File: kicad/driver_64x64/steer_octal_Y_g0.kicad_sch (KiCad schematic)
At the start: 66 parts

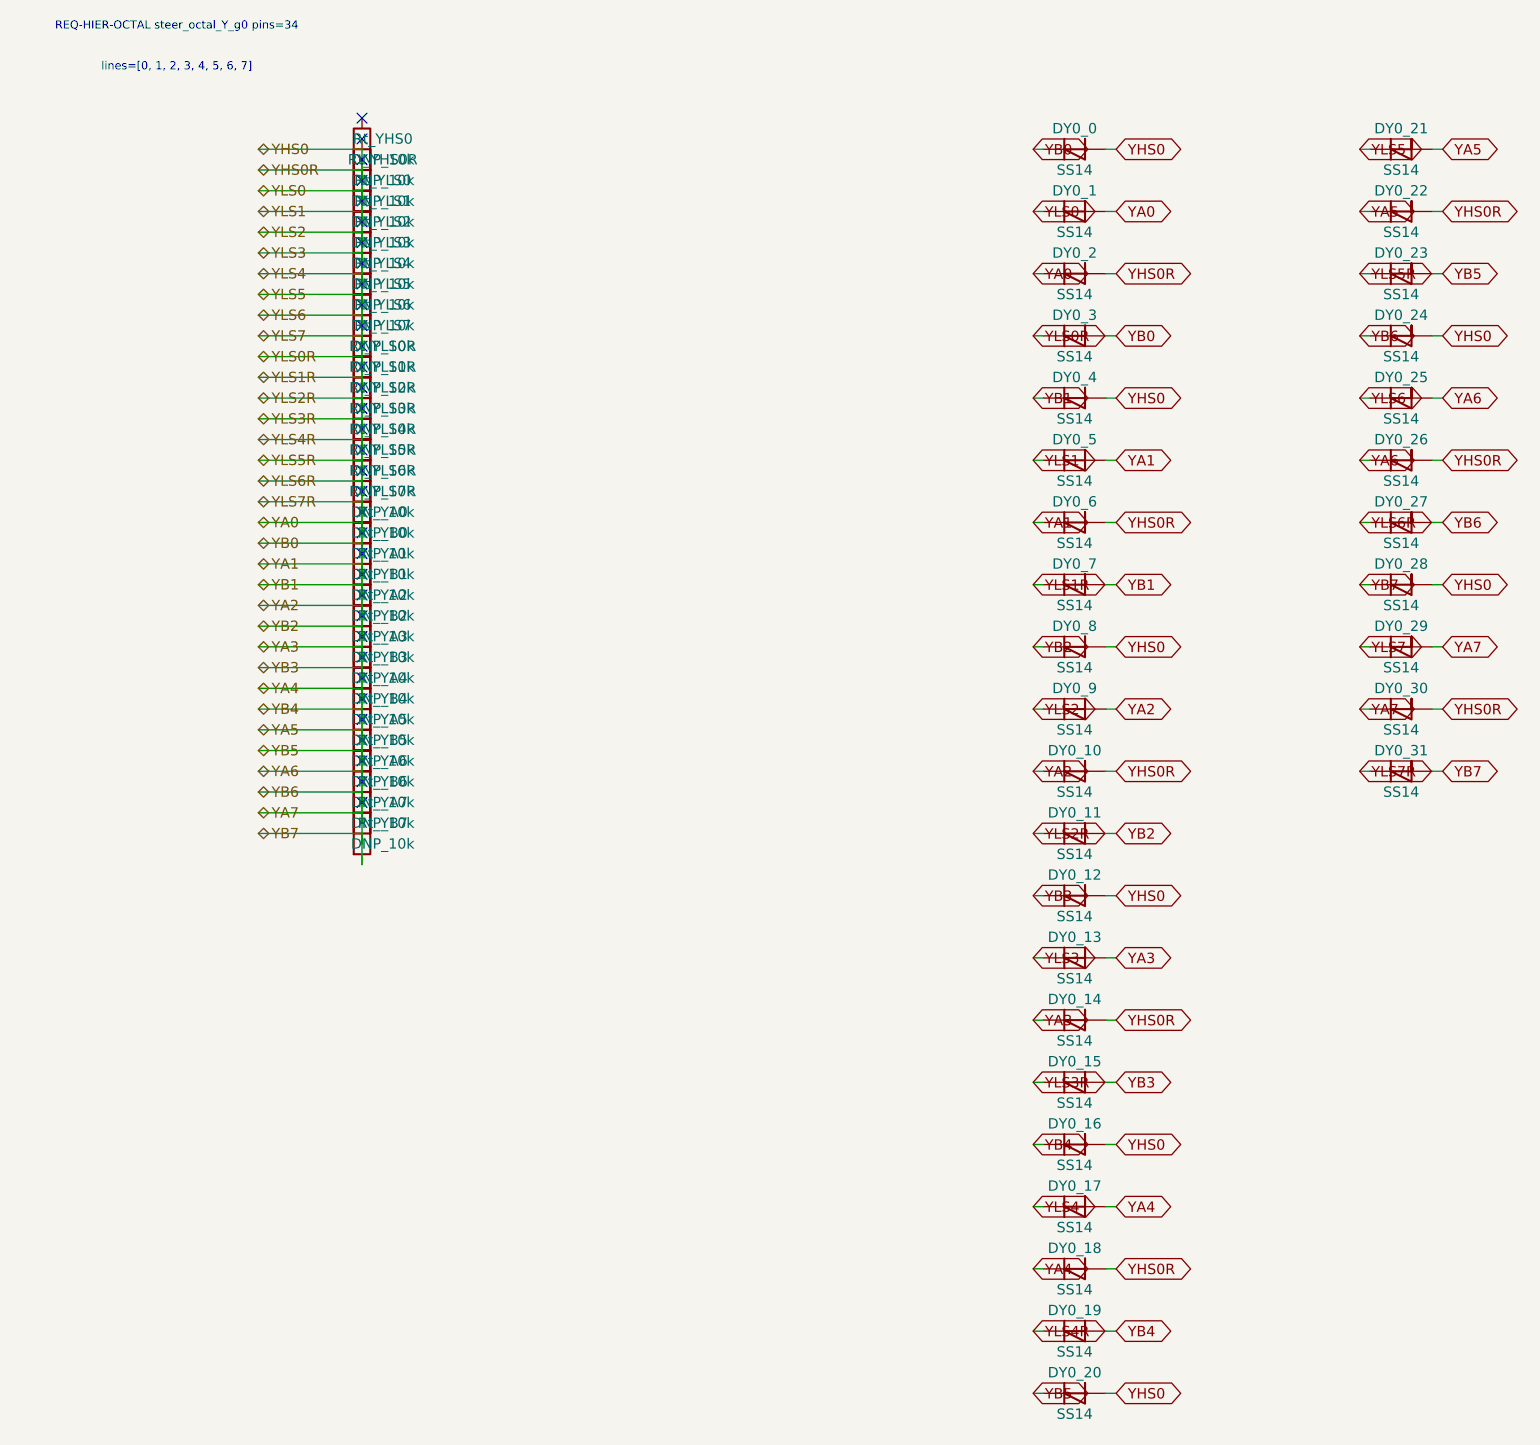
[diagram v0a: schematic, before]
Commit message: logical seperation into host and multiple decode/drive/steering boards
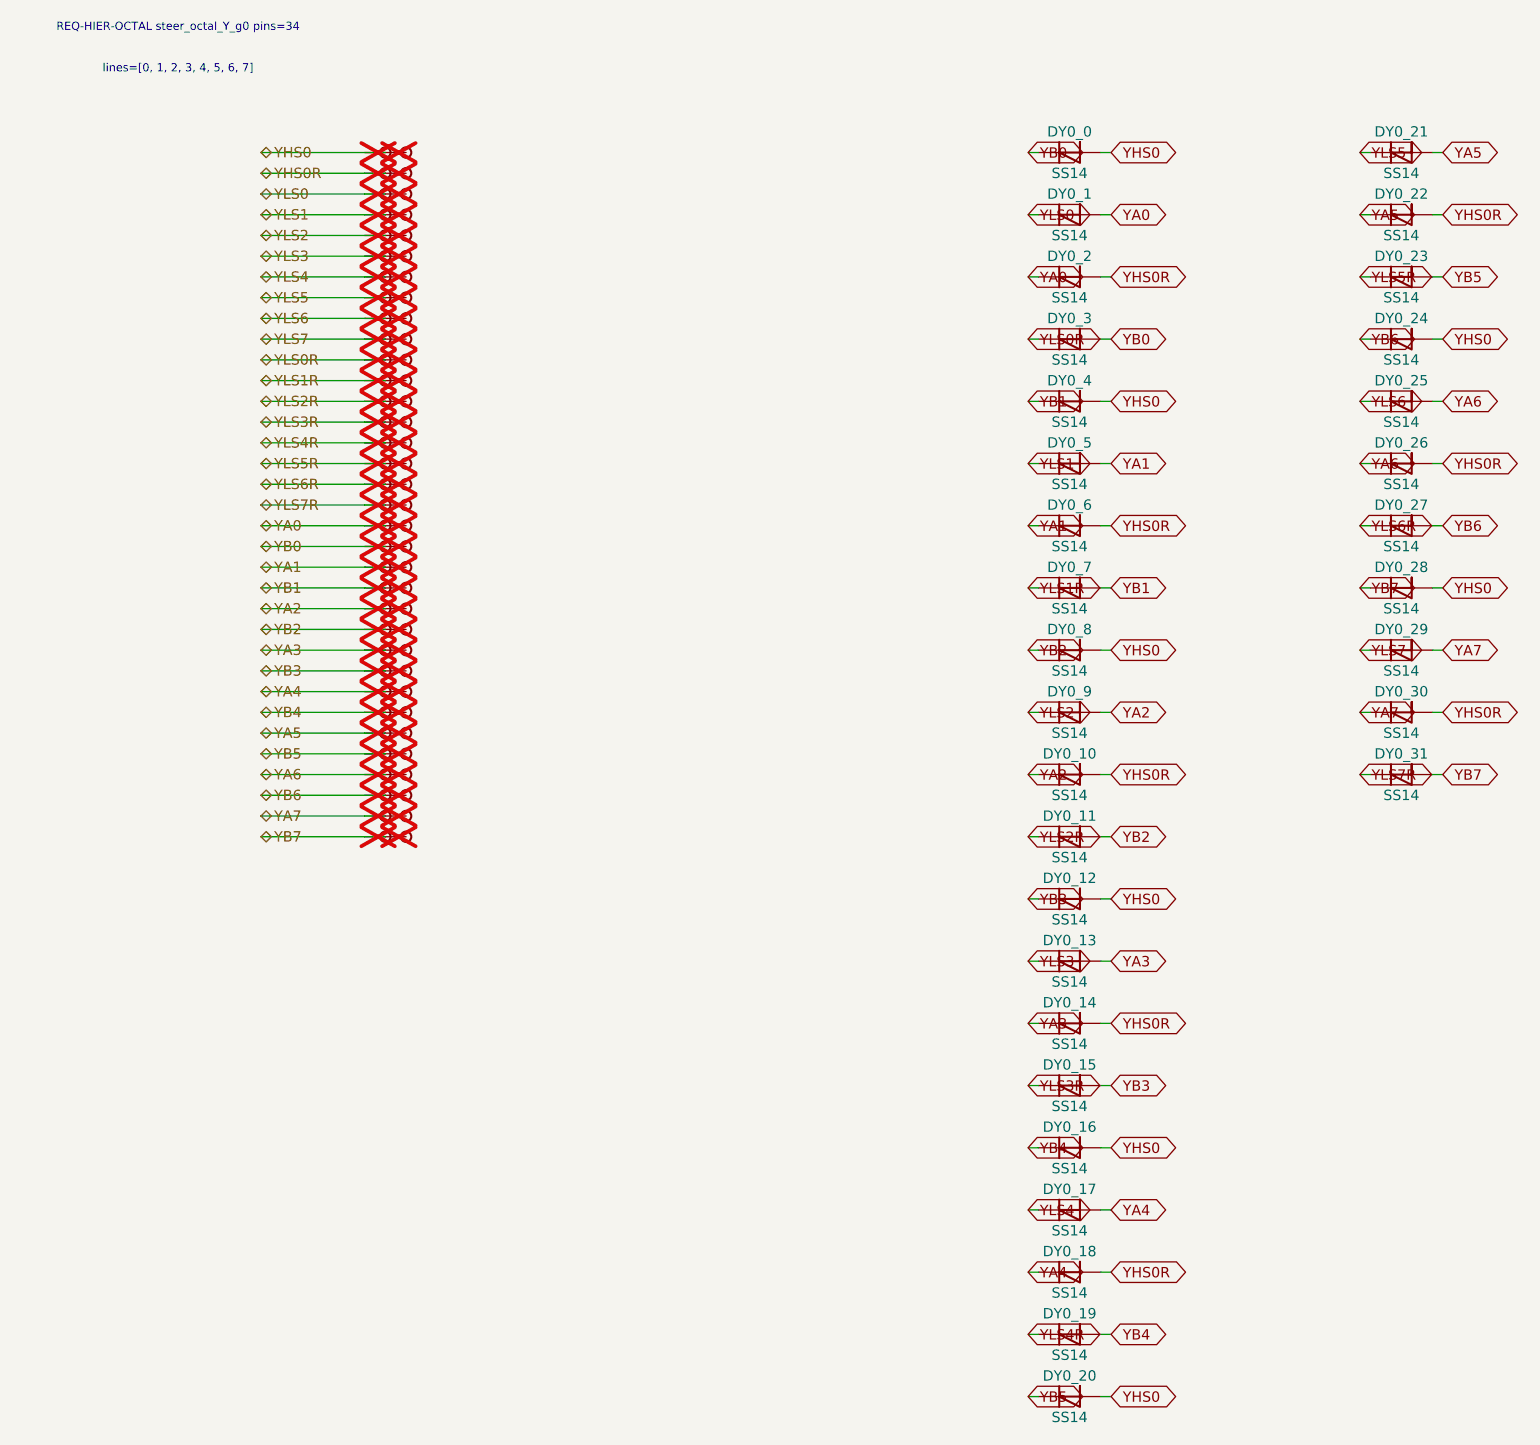
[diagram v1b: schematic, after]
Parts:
- removed Rt_YA0, Rt_YA1, Rt_YA2, Rt_YA3, Rt_YA4, Rt_YA5, Rt_YA6, Rt_YA7, Rt_YB0, Rt_YB1, Rt_YB2, Rt_YB3, Rt_YB4, Rt_YB5, Rt_YB6, Rt_YB7, Rt_YHS0, Rt_YHS0R, Rt_YLS0, Rt_YLS0R, Rt_YLS1, Rt_YLS1R, Rt_YLS2, Rt_YLS2R, Rt_YLS3, Rt_YLS3R, Rt_YLS4, Rt_YLS4R, Rt_YLS5, Rt_YLS5R, Rt_YLS6, Rt_YLS6R, Rt_YLS7, Rt_YLS7R: DNP_10k, symbol Device:R
- added TP_YA0, TP_YA0b, TP_YA1, TP_YA1b, TP_YA2, TP_YA2b, TP_YA3, TP_YA3b, TP_YA4, TP_YA4b, TP_YA5, TP_YA5b, TP_YA6, TP_YA6b, TP_YA7, TP_YA7b, TP_YB0, TP_YB0b, TP_YB1, TP_YB1b, TP_YB2, TP_YB2b, TP_YB3, TP_YB3b, TP_YB4, TP_YB4b, TP_YB5, TP_YB5b, TP_YB6, TP_YB6b, TP_YB7, TP_YB7b, TP_YHS0, TP_YHS0R, TP_YHS0Rb, TP_YHS0b, TP_YLS0, TP_YLS0R, TP_YLS0Rb, TP_YLS0b, TP_YLS1, TP_YLS1R, TP_YLS1Rb, TP_YLS1b, TP_YLS2, TP_YLS2R, TP_YLS2Rb, TP_YLS2b, TP_YLS3, TP_YLS3R, TP_YLS3Rb, TP_YLS3b, TP_YLS4, TP_YLS4R, TP_YLS4Rb, TP_YLS4b, TP_YLS5, TP_YLS5R, TP_YLS5Rb, TP_YLS5b, TP_YLS6, TP_YLS6R, TP_YLS6Rb, TP_YLS6b, TP_YLS7, TP_YLS7R, TP_YLS7Rb, TP_YLS7b: Stub, symbol CMR:Stub
- DY0_0, DY0_1, DY0_10, DY0_11, DY0_12, DY0_13, DY0_14, DY0_15, DY0_16, DY0_17, DY0_18, DY0_19, DY0_2, DY0_20, DY0_21, DY0_22, DY0_23, DY0_24, DY0_25, DY0_26, DY0_27, DY0_28, DY0_29, DY0_3, DY0_30, DY0_31, DY0_4, DY0_5, DY0_6, DY0_7, DY0_8, DY0_9: symbol Device:D_Schottky -> CMR:D_Schottky
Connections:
- net YA0: now also TP_YA0.1, TP_YA0b.1; no longer DY0_0.1 (K), DY0_0.2 (A), DY0_1.1 (K), DY0_10.1 (K), DY0_10.2 (A), DY0_11.1 (K), DY0_11.2 (A), DY0_12.1 (K), DY0_12.2 (A), DY0_13.1 (K), DY0_13.2 (A), DY0_14.1 (K), DY0_14.2 (A), DY0_15.1 (K), DY0_15.2 (A), DY0_16.1 (K), DY0_16.2 (A), DY0_17.1 (K), DY0_17.2 (A), DY0_18.1 (K), DY0_18.2 (A), DY0_19.1 (K), DY0_19.2 (A), DY0_2.2 (A), DY0_20.1 (K), DY0_20.2 (A), DY0_21.1 (K), DY0_21.2 (A), DY0_22.1 (K), DY0_22.2 (A), DY0_23.1 (K), DY0_23.2 (A), DY0_24.1 (K), DY0_24.2 (A), DY0_25.1 (K), DY0_25.2 (A), DY0_26.1 (K), DY0_26.2 (A), DY0_27.1 (K), DY0_27.2 (A), DY0_28.1 (K), DY0_28.2 (A), DY0_29.1 (K), DY0_29.2 (A), DY0_3.1 (K), DY0_3.2 (A), DY0_30.1 (K), DY0_30.2 (A), DY0_31.1 (K), DY0_31.2 (A), DY0_4.1 (K), DY0_4.2 (A), DY0_5.1 (K), DY0_5.2 (A), DY0_6.1 (K), DY0_6.2 (A), DY0_7.1 (K), DY0_7.2 (A), DY0_8.1 (K), DY0_8.2 (A), DY0_9.1 (K), DY0_9.2 (A)
- new net YA1: DY0_5.2 (A), DY0_6.1 (K), TP_YA1.1, TP_YA1b.1
- new net YA2: DY0_10.1 (K), DY0_9.2 (A), TP_YA2.1, TP_YA2b.1
- new net YA3: DY0_13.2 (A), DY0_14.1 (K), TP_YA3.1, TP_YA3b.1
- new net YA4: DY0_17.2 (A), DY0_18.1 (K), TP_YA4.1, TP_YA4b.1
- new net YA5: DY0_21.2 (A), DY0_22.1 (K), TP_YA5.1, TP_YA5b.1
- new net YA6: DY0_25.2 (A), DY0_26.1 (K), TP_YA6.1, TP_YA6b.1
- new net YA7: DY0_29.2 (A), DY0_30.1 (K), TP_YA7.1, TP_YA7b.1
- new net YB0: DY0_0.1 (K), DY0_3.2 (A), TP_YB0.1, TP_YB0b.1
- new net YB1: DY0_4.1 (K), DY0_7.2 (A), TP_YB1.1, TP_YB1b.1
- new net YB2: DY0_11.2 (A), DY0_8.1 (K), TP_YB2.1, TP_YB2b.1
- new net YB3: DY0_12.1 (K), DY0_15.2 (A), TP_YB3.1, TP_YB3b.1
- new net YB4: DY0_16.1 (K), DY0_19.2 (A), TP_YB4.1, TP_YB4b.1
- new net YB5: DY0_20.1 (K), DY0_23.2 (A), TP_YB5.1, TP_YB5b.1
- new net YB6: DY0_24.1 (K), DY0_27.2 (A), TP_YB6.1, TP_YB6b.1
- new net YB7: DY0_28.1 (K), DY0_31.2 (A), TP_YB7.1, TP_YB7b.1
- new net YHS0: DY0_0.2 (A), DY0_12.2 (A), DY0_16.2 (A), DY0_20.2 (A), DY0_24.2 (A), DY0_28.2 (A), DY0_4.2 (A), DY0_8.2 (A), TP_YHS0.1, TP_YHS0b.1
- new net YHS0R: DY0_10.2 (A), DY0_14.2 (A), DY0_18.2 (A), DY0_2.2 (A), DY0_22.2 (A), DY0_26.2 (A), DY0_30.2 (A), DY0_6.2 (A), TP_YHS0R.1, TP_YHS0Rb.1
- new net YLS0: DY0_1.1 (K), TP_YLS0.1, TP_YLS0b.1
- new net YLS0R: DY0_3.1 (K), TP_YLS0R.1, TP_YLS0Rb.1
- new net YLS1: DY0_5.1 (K), TP_YLS1.1, TP_YLS1b.1
- new net YLS1R: DY0_7.1 (K), TP_YLS1R.1, TP_YLS1Rb.1
- new net YLS2: DY0_9.1 (K), TP_YLS2.1, TP_YLS2b.1
- new net YLS2R: DY0_11.1 (K), TP_YLS2R.1, TP_YLS2Rb.1
- new net YLS3: DY0_13.1 (K), TP_YLS3.1, TP_YLS3b.1
- new net YLS3R: DY0_15.1 (K), TP_YLS3R.1, TP_YLS3Rb.1
- new net YLS4: DY0_17.1 (K), TP_YLS4.1, TP_YLS4b.1
- new net YLS4R: DY0_19.1 (K), TP_YLS4R.1, TP_YLS4Rb.1
- new net YLS5: DY0_21.1 (K), TP_YLS5.1, TP_YLS5b.1
- new net YLS5R: DY0_23.1 (K), TP_YLS5R.1, TP_YLS5Rb.1
- new net YLS6: DY0_25.1 (K), TP_YLS6.1, TP_YLS6b.1
- new net YLS6R: DY0_27.1 (K), TP_YLS6R.1, TP_YLS6Rb.1
- new net YLS7: DY0_29.1 (K), TP_YLS7.1, TP_YLS7b.1
- new net YLS7R: DY0_31.1 (K), TP_YLS7R.1, TP_YLS7Rb.1
- no-connect marks 34 -> 0
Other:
- moved on the sheet: DY0_0, DY0_1, DY0_10, DY0_11, DY0_12, DY0_13, DY0_14, DY0_15, DY0_16, DY0_17, DY0_18, DY0_19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
